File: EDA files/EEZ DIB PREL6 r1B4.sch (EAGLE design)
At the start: 67 parts, among them IC1 STM32F030C6T6, IC2 74HC1G126GW,125, IC3 M24C32-WMN6P, IC4 LP2985-33DBVR, K1 RT424005, K2 RT424005, K3 RT424005, K4 RT424005, K5 RT424005, K6 RT424005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

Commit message: #4, OSHW UID
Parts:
- removed ZD2, ZD3, ZD4, ZD5, ZD6: MM3Z18VT1G, EEZ_Lib1:ZENER-DIODESOD323R
- added FM3: FIDUCIAL_2, EEZ_Lib1:FIDUCIAL_2
- added U$3: HR000005, OSHWA:CERT-SMALL
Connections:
- removed net N$10: D5.A, ZD5.A
- removed net N$6: D3.A, ZD3.A
- removed net N$8: D4.A, ZD4.A
- removed net N$9: K4K.C2, Q4.D, ZD4.C
- removed net N$98: D6.A, ZD6.A
- net +5V: now also ZD1.A; no longer D1.C, D2.C, D3.C, D4.C, D5.C, D6.C
- net N$1: now also D4.A, K4K.C2, Q4.D; no longer D1.A, ZD1.A
- net N$100: now also D6.A; no longer ZD6.C
- net N$11: now also D5.A; no longer ZD5.C
- net N$2: now also D1.A; no longer ZD1.C
- net N$3: now also D1.C, D2.C, D3.C, D4.C, D5.C, D6.C, ZD1.C; no longer D2.A, ZD2.A
- net N$4: now also D2.A; no longer ZD2.C
- net N$7: now also D3.A; no longer ZD3.C
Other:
- moved on the sheet: D1, D2, D3, D4, D5, D6, ZD1

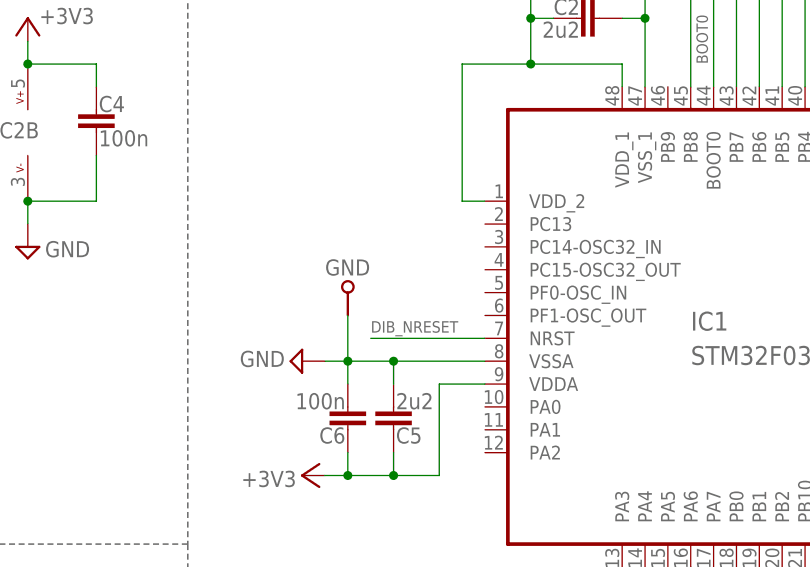
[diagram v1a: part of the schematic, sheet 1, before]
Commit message: PCB ID added
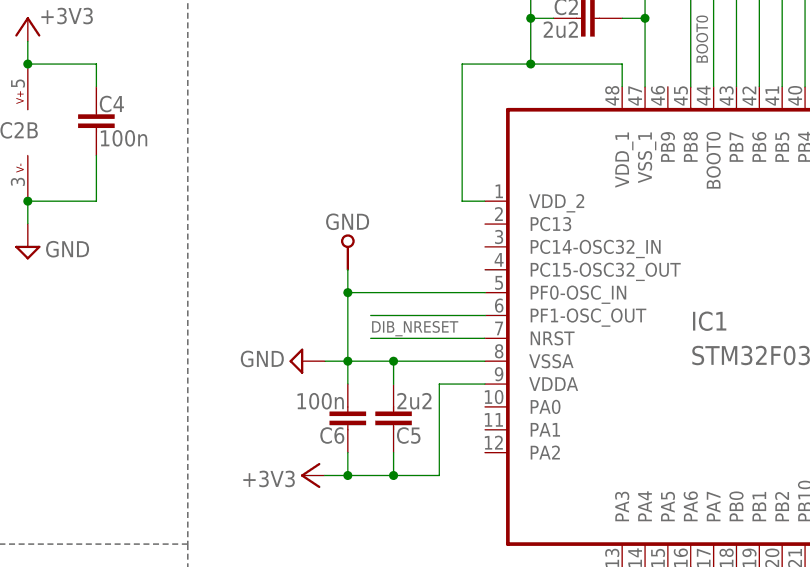
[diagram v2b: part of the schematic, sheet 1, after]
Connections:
- new net N$6: IC1.PF1-OSC_OUT
- net GND: now also IC1.PF0-OSC_IN
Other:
- note added: "PCB_ID0"
- note added: "PCB_ID1"
- note added: "PCB_ID=1"
- moved on the sheet: GND
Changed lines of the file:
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@@
 <text x="144.78" y="175.26" size="1.778" layer="97">JTAG/SWD (optional)</text>
 <text x="7.62" y="175.26" size="1.778" layer="97">DIB connector</text>
+<text x="162.56" y="94.615" size="1.27" layer="103">PCB_ID0</text>
+<text x="162.56" y="92.075" size="1.27" layer="103">PCB_ID1</text>
+<text x="147.32" y="94.615" size="1.27" layer="103">PCB_ID=1</text>
 </plain>
 <instances>
@@
 <attribute name="VALUE" x="153.035" y="85.725" size="1.778" layer="96" rot="MR0"/>
 </instance>
-<instance part="GND" gate="G$1" x="160.02" y="93.98" smashed="yes" rot="R90">
-<attribute name="NAME" x="157.48" y="95.885" size="1.778" layer="95"/>
-<attribute name="VALUE" x="162.56" y="93.98" size="1.778" layer="96" rot="R90"/>
+<instance part="GND" gate="G$1" x="160.02" y="99.06" smashed="yes" rot="R90">
+<attribute name="NAME" x="157.48" y="100.965" size="1.778" layer="95"/>
+<attribute name="VALUE" x="162.56" y="99.06" size="1.778" layer="96" rot="R90"/>
 </instance>
 <instance part="DIB1.1" gate="G$1" x="251.46" y="104.14" smashed="yes" rot="MR0">
@@
 <junction x="160.02" y="86.36"/>
 <pinref part="GND" gate="G$1" pin="P$1"/>
-<wire x1="160.02" y1="86.36" x2="160.02" y2="91.44" width="0.1524" layer="91"/>
+<wire x1="160.02" y1="86.36" x2="160.02" y2="93.98" width="0.1524" layer="91"/>
+<pinref part="IC1" gate="G$1" pin="PF0-OSC_IN"/>
+<wire x1="160.02" y1="93.98" x2="160.02" y2="96.52" width="0.1524" layer="91"/>
+<wire x1="175.26" y1="93.98" x2="160.02" y2="93.98" width="0.1524" layer="91"/>
+<junction x="160.02" y="93.98"/>
 </segment>
 <segment>
@@
 </segment>
 </net>
+<net name="N$6" class="0">
+<segment>
+<pinref part="IC1" gate="G$1" pin="PF1-OSC_OUT"/>
+<wire x1="175.26" y1="91.44" x2="162.56" y2="91.44" width="0.1524" layer="91"/>
+</segment>
+</net>
